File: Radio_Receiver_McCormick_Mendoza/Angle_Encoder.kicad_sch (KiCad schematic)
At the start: 7 parts, among them SW1 RotaryEncoder_Switch_MP

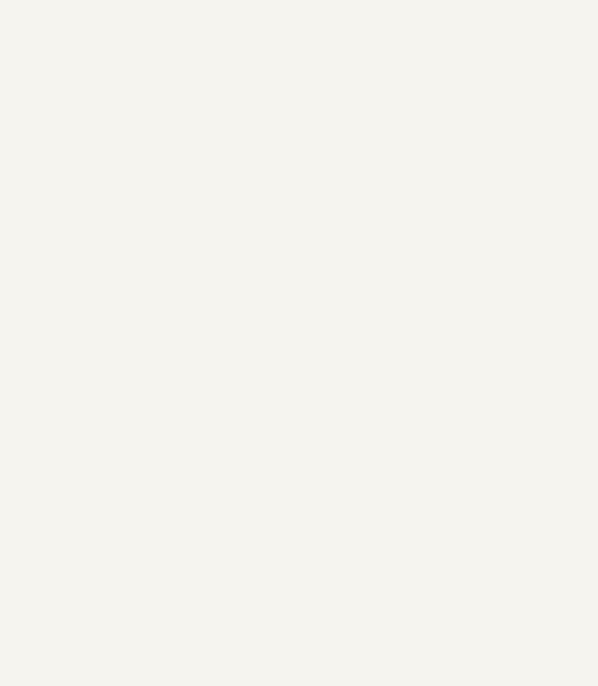
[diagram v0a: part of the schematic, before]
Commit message: Added digital power regulator
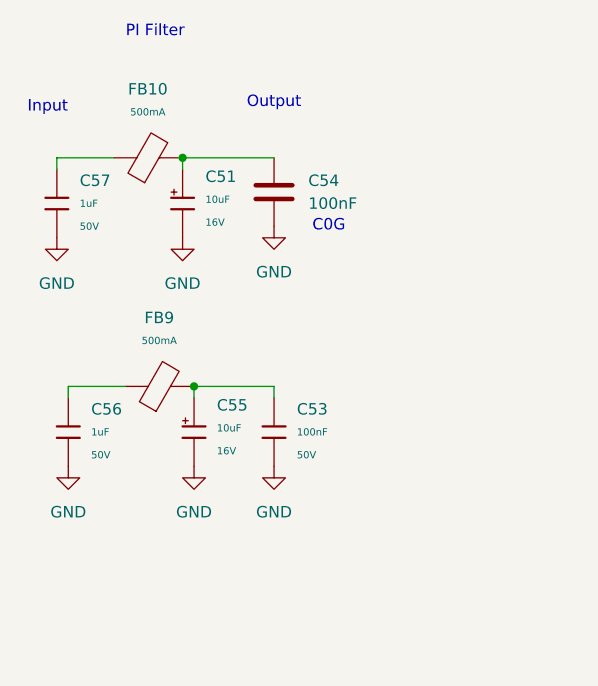
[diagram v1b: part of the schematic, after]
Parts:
- added C51, C55: 10uF, PCM_JLCPCB:C_CASE-A-3216-18(mm), symbol PCM_JLCPCB-Capacitors:CASE-A-3216-18(mm),10uF
- added C53: 100nF, PCM_JLCPCB:C_0402, symbol PCM_JLCPCB-Capacitors:0402,100nF,(2)
- added C54: 100nF, PCM_JLCPCB:C_1206, symbol Device:C
- added C56, C57: 1uF, PCM_JLCPCB:C_0603, symbol PCM_JLCPCB-Capacitors:0603,1uF
- added FB10, FB9: (no value), PCM_JLCPCB:FB_0805, symbol PCM_JLCPCB-Inductors:Ferrite,0805,(2)
- C35, C36, C38: Manufacturer Samsung Electro-Mechanics -> (none)
- R7, R8, R9: Manufacturer UNI-ROYAL(Uniroyal Elec) -> (none)
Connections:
- net GND: now also C51.2, C53.2, C54.2, C55.2, C56.2, C57.2
- new net: C53.1, C55.1, FB9.2
- new net: C57.1, FB10.1
- new net: C51.1, C54.1, FB10.2
- new net: C56.1, FB9.1
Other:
- note added: "C0G"
- note added: "Input"
- note added: "Output"
- note added: "PI Filter"

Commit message: Integrated signal path modules
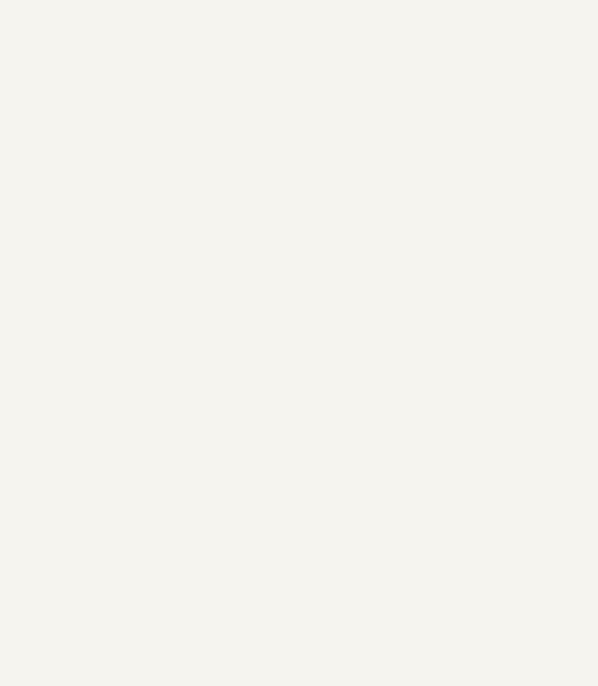
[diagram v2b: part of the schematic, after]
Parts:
- removed C51, C55: 10uF, PCM_JLCPCB:C_CASE-A-3216-18(mm), symbol PCM_JLCPCB-Capacitors:CASE-A-3216-18(mm),10uF
- removed C53: 100nF, PCM_JLCPCB:C_0402, symbol PCM_JLCPCB-Capacitors:0402,100nF,(2)
- removed C54: 100nF, PCM_JLCPCB:C_1206, symbol Device:C
- removed C56, C57: 1uF, PCM_JLCPCB:C_0603, symbol PCM_JLCPCB-Capacitors:0603,1uF
- removed FB10, FB9: (no value), PCM_JLCPCB:FB_0805, symbol PCM_JLCPCB-Inductors:Ferrite,0805,(2)
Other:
- note removed: "C0G"
- note removed: "Input"
- note removed: "Output"
- note removed: "PI Filter"
